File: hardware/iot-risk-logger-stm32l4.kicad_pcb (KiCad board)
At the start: 2 copper layers, 55 x 45 mm, 52 parts, among them J1 USB Type-C, J2 TagConnect SWD ARM, Q1 IRLML6401, U1 ST25DV04K, U2 OPT3001DNPR, U3 SHT30-DIS, U4 LIS2DW12, U5 AP2112K-3.3, U6 W25Q64JV, U7 STM32L412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

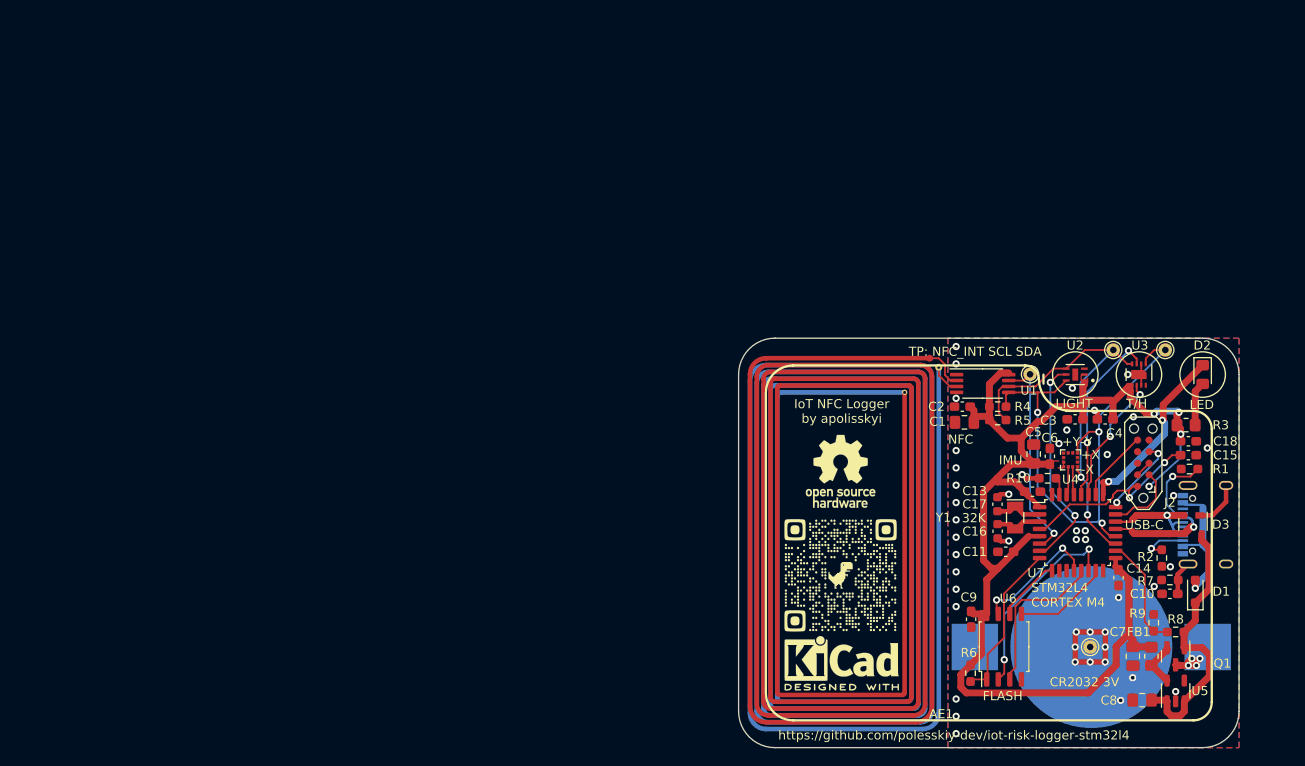
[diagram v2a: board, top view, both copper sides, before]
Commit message: PCB: paint in different colours
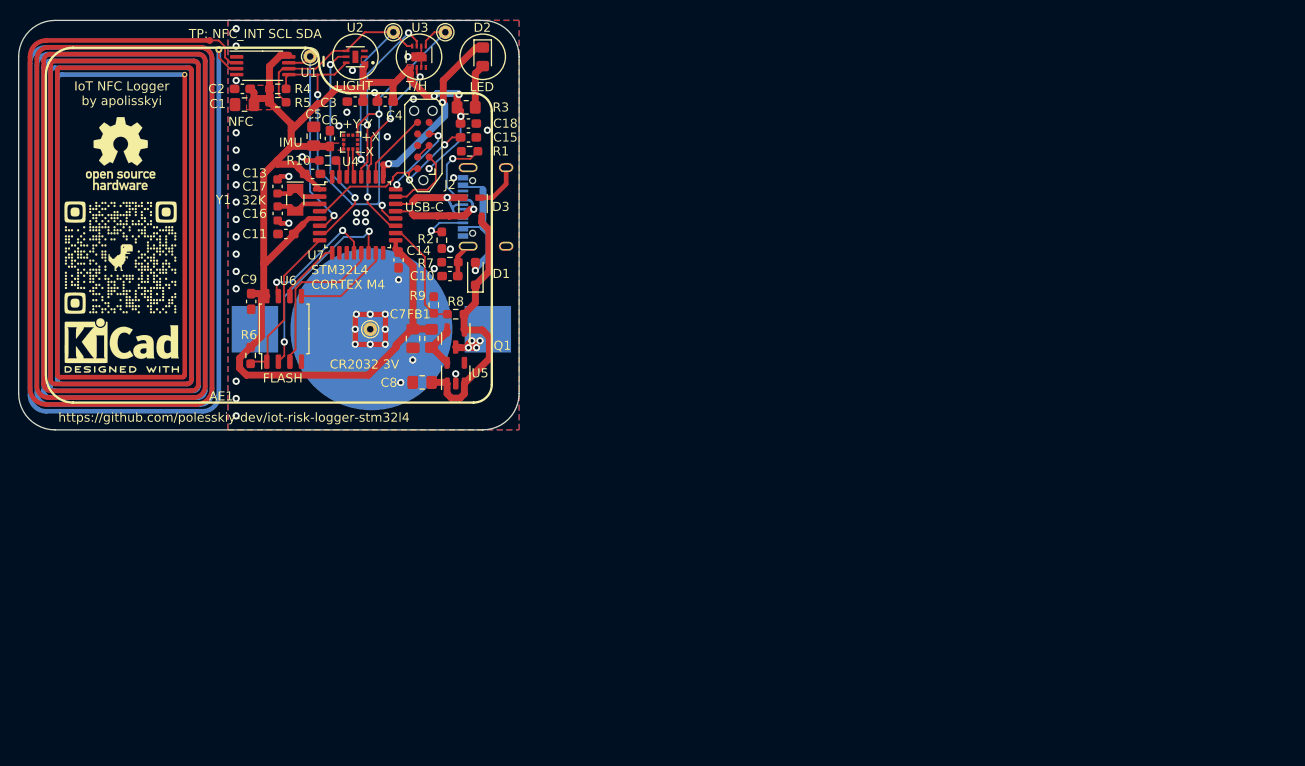
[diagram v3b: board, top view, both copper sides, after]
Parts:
- moved REF97 87.9 mm to (37.3, 48.0)
- moved C11 86.5 mm to (55.2, 46.1)
- moved C17 86.5 mm to (54.3, 40.8)
- moved AE1 86.5 mm to (37.6, 45.5)
- moved BT1 86.5 mm to (64.6, 56.5)
- moved C10 86.5 mm to (73.3, 50.7)
- moved C14 86.5 mm to (67.6, 48.9)
- moved C15 86.5 mm to (75.3, 35.4)
- moved C16 86.5 mm to (54.3, 43.8)
- moved C18 86.5 mm to (75.3, 33.9)
- moved C3 86.5 mm to (62.9, 31.5)
- moved C4 86.5 mm to (66.2, 31.5)
- moved C5 86.5 mm to (58.3, 35.3)
- moved C7 86.5 mm to (69.2, 57.5)
- moved C8 86.5 mm to (70.2, 62.4)
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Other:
- board text added: "0.0000 mm / 0.0000 mm"
- board text added: "0.3000 mm"
- board text added: "1.6000 mm"
- board text added: "2"
- board text added: "55.0000 mm x 45.0000 mm"
- board text added: "BOARD CHARACTERISTICS"
- board text added: "Board Thickness:"
- board text added: "Board overall dimensions:"
- board text added: "Castellated pads:"
- board text added: "Copper Finish:"
- board text added: "Copper Layer Count:"
- board text added: "Edge card connectors:"
- board text added: "Impedance Control:"
- board text added: "Min hole diameter:"
- board text added: "Min track/spacing:"
- board text added: "No"
- board text added: "None"
- board text added: "Plated Board Edge:"
- board text added: "REV 1.0.0"

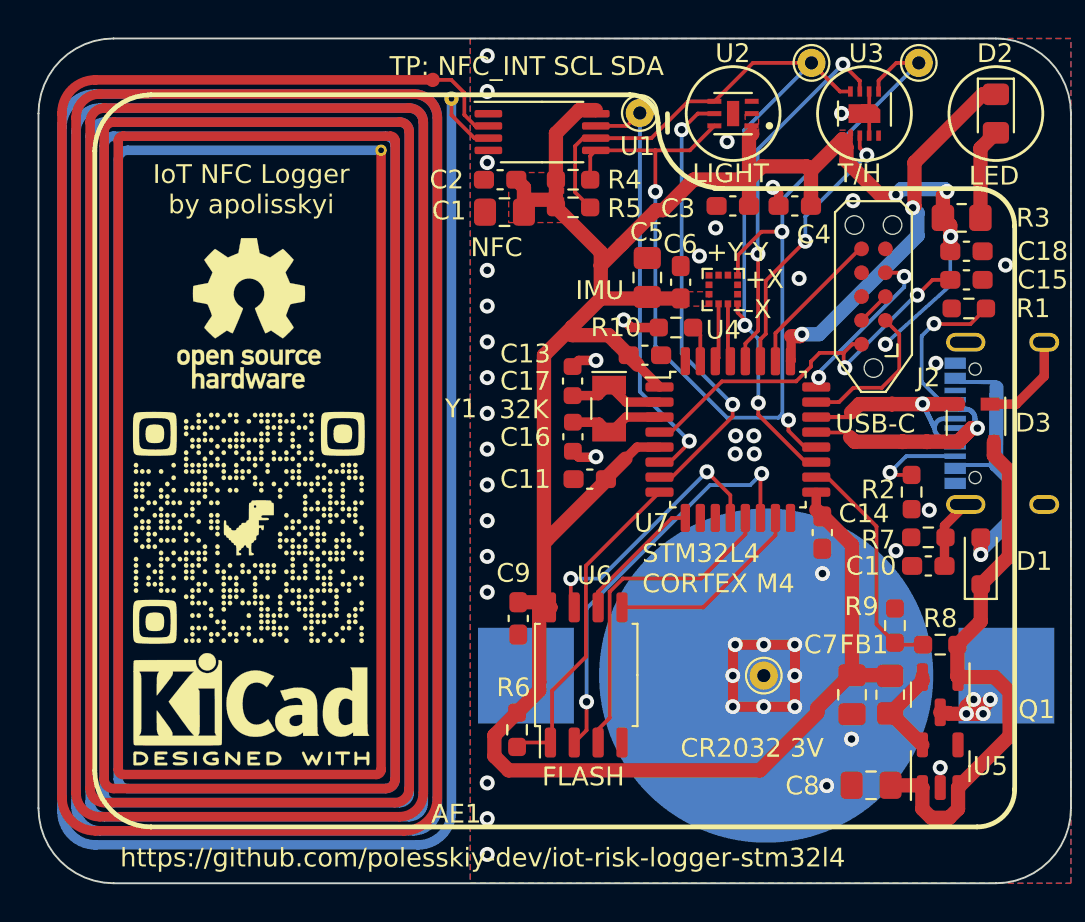
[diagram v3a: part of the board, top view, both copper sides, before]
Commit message: PCB: add colours and board extraction cutout
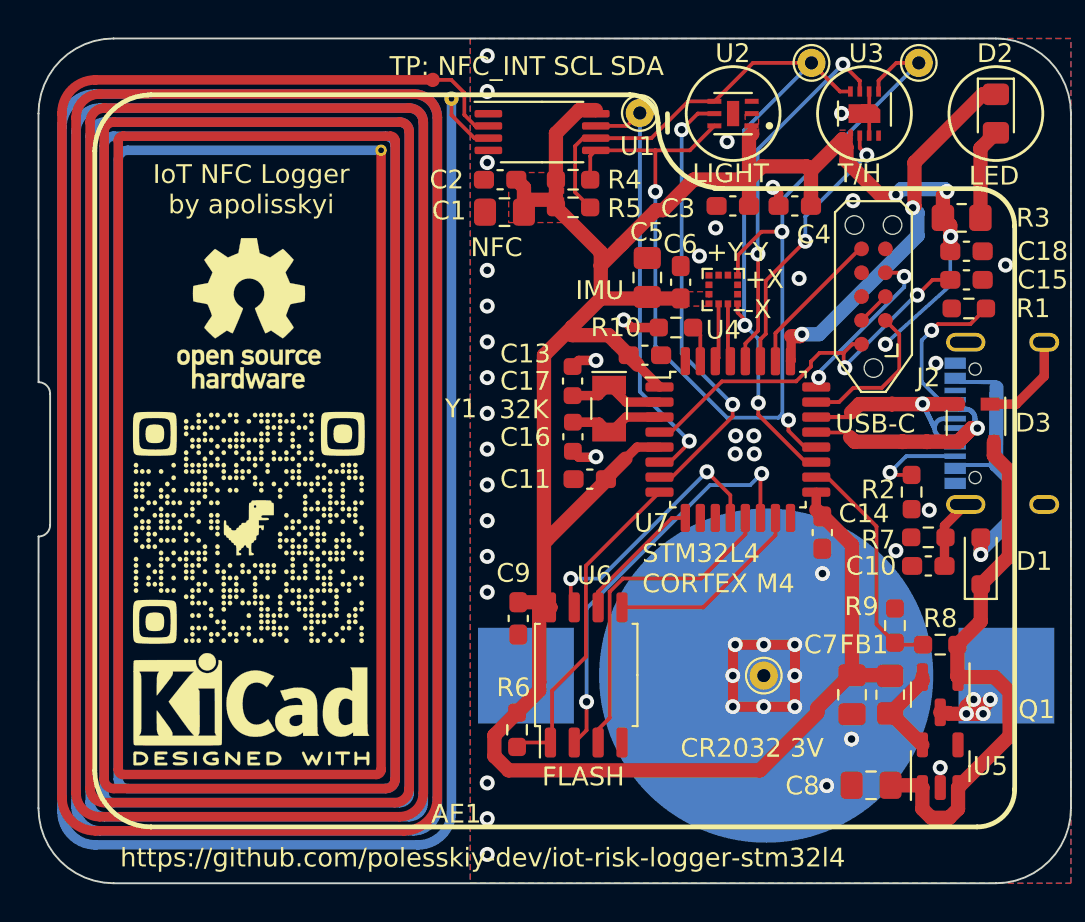
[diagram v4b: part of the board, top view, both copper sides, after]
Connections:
- J1 pad s1: (no net) -> /GND_SHIELD
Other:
- outline, holes or cut-outs redrawn
